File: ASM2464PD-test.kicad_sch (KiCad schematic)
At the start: 19 parts, among them J1 USB_C_Receptacle, J2 Bus_M.2_Socket_M

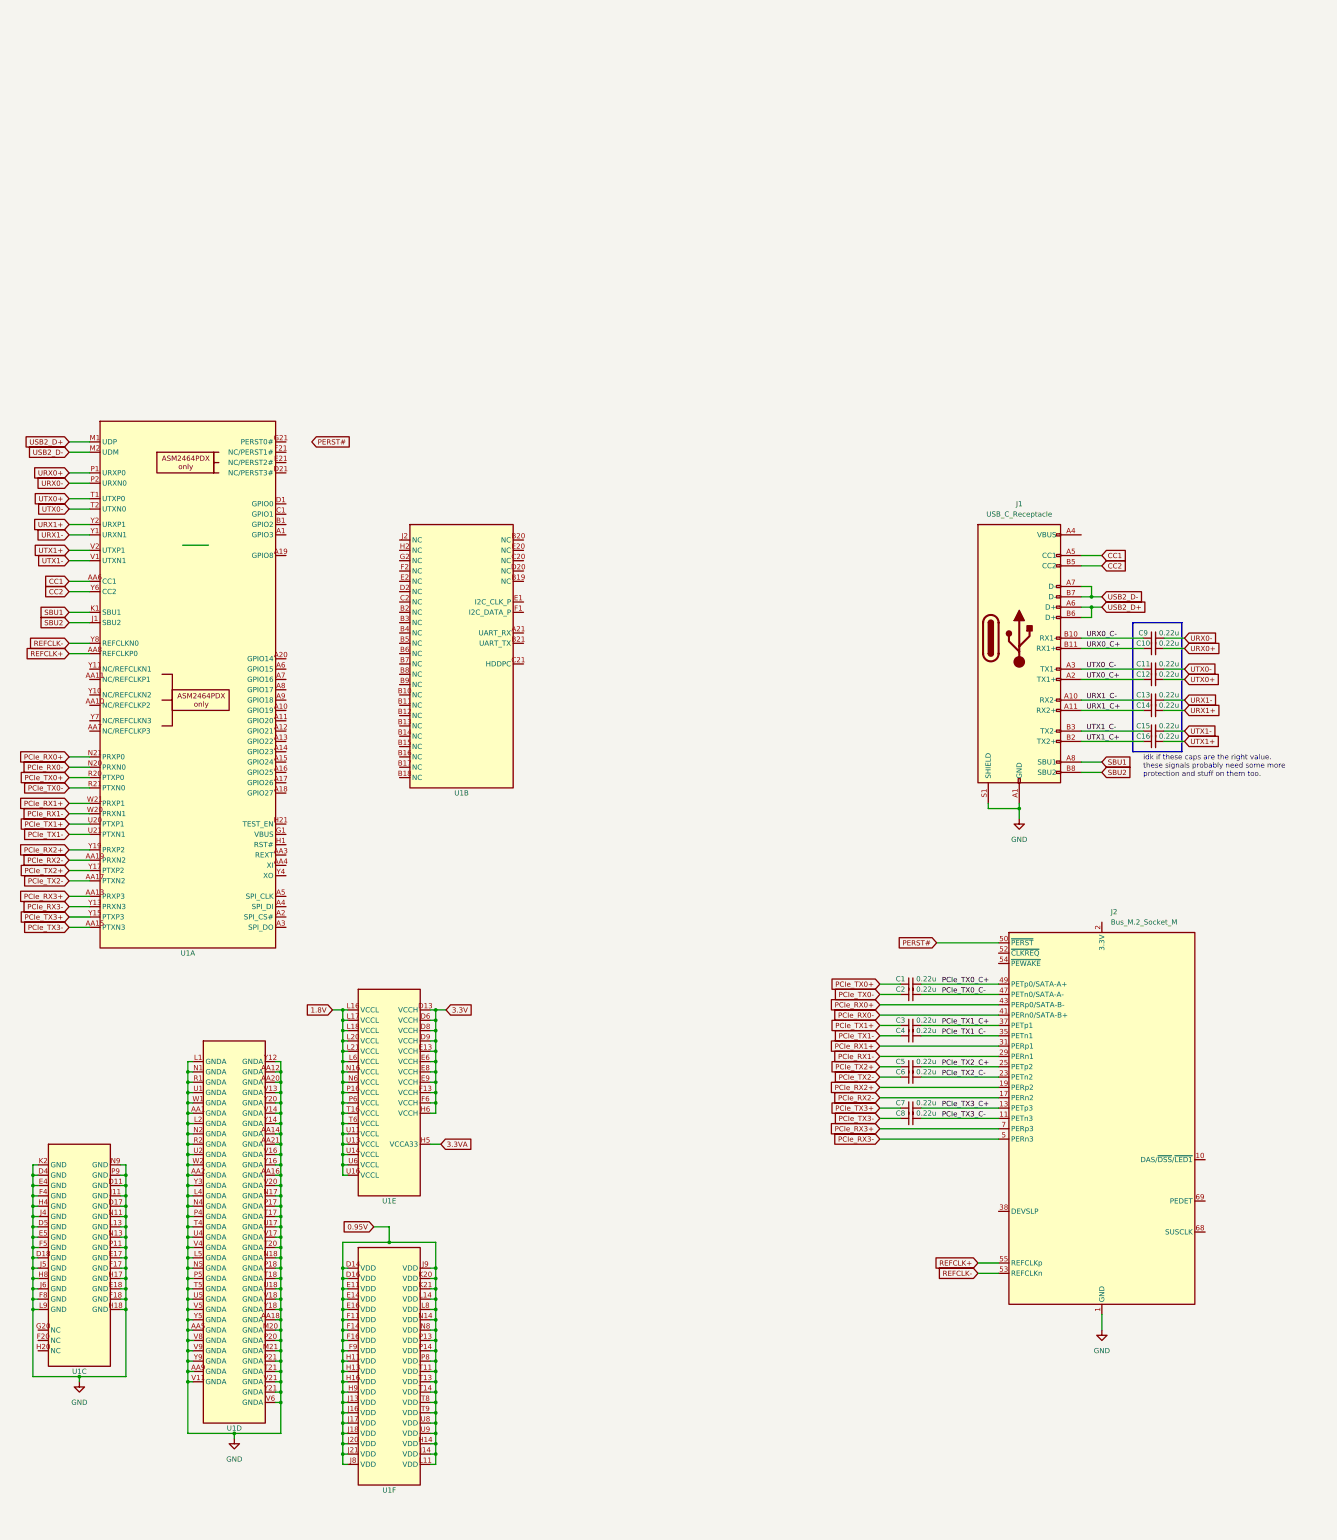
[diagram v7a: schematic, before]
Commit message: Updated schematic and rerouted some stuff
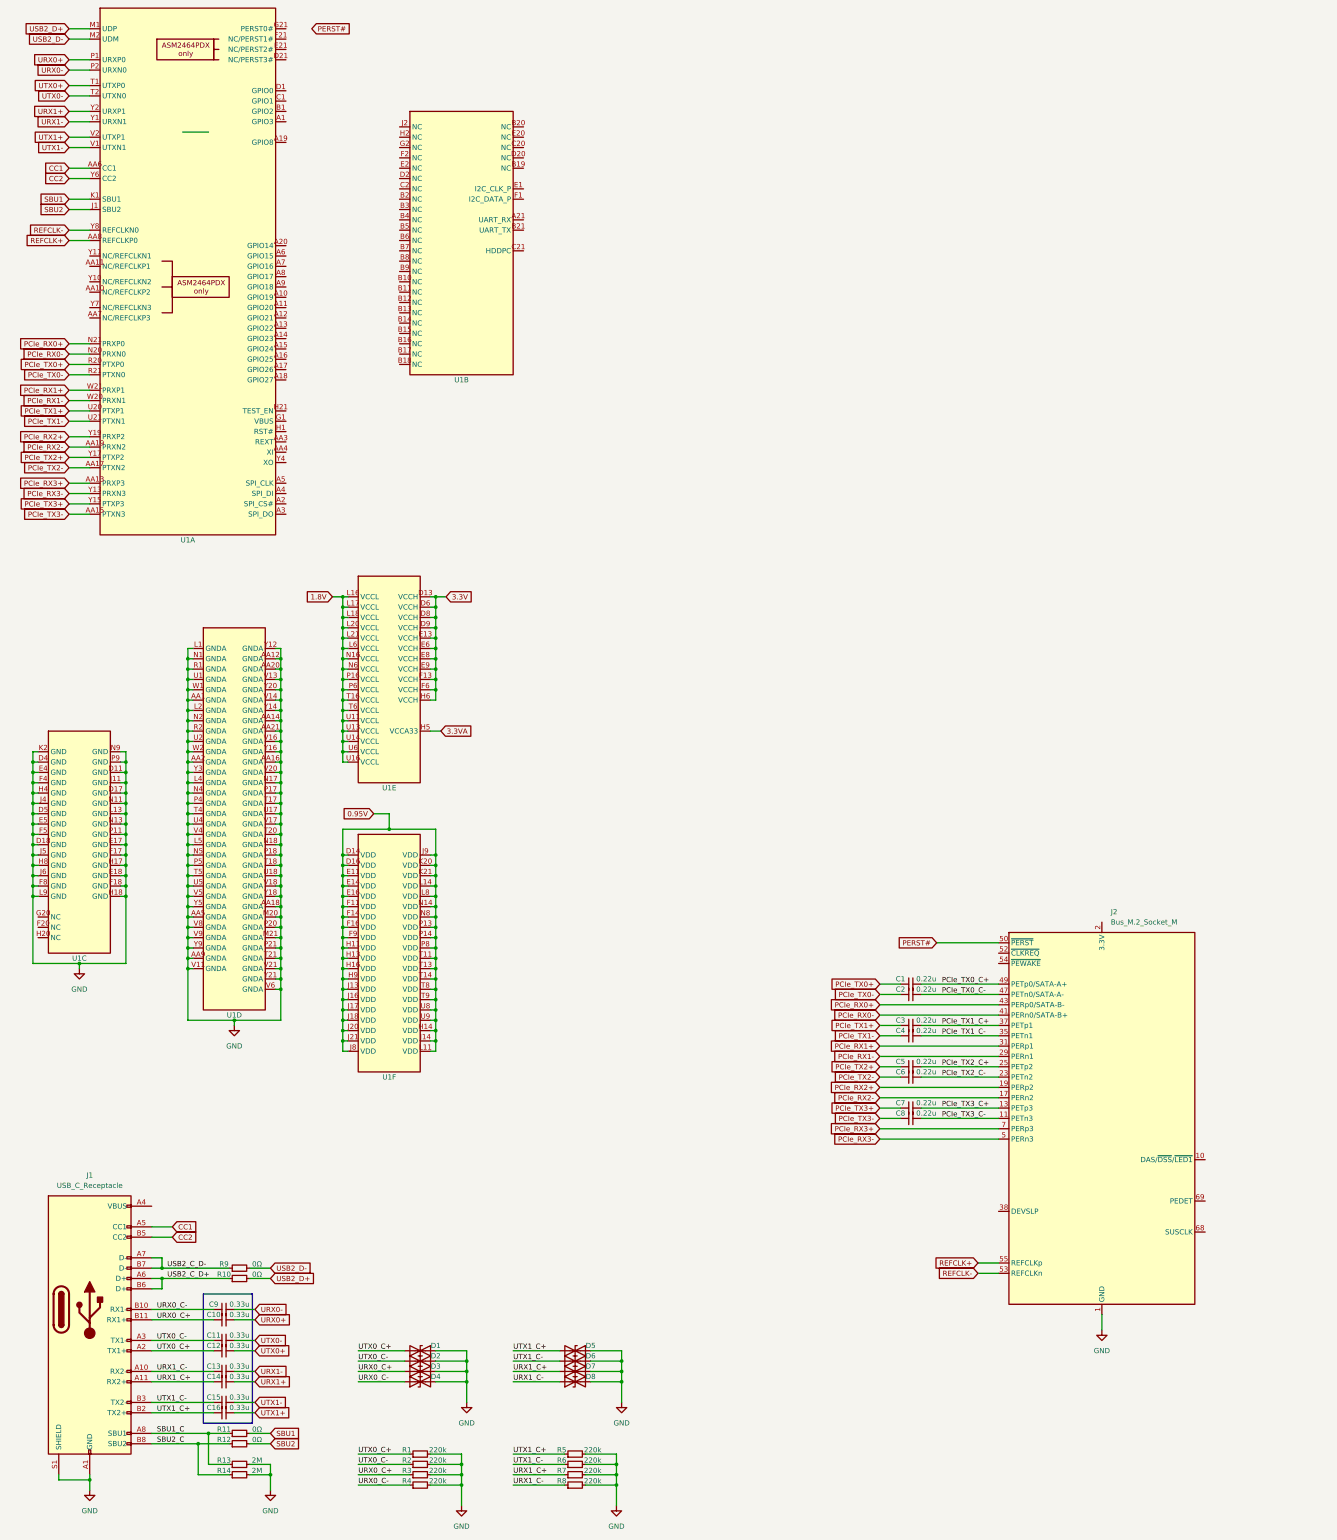
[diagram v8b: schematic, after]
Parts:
- added D1, D2, D3, D4, D5, D6, D7, D8: ~, Diode_SMD:D_0201_0603Metric, symbol Diode:ESD9B3.3ST5G
- added R1, R2, R3, R4, R5, R6, R7, R8: 220k, Resistor_SMD:R_0201_0603Metric, symbol Device:R_Small
- added R10, R11, R12, R9: 0Ω, Resistor_SMD:R_0201_0603Metric, symbol Device:R_Small
- added R13, R14: 2M, Resistor_SMD:R_0201_0603Metric, symbol Device:R_Small
- C10, C11, C12, C13, C14, C15, C16, C9: value 0.22u -> 0.33u; footprint Capacitor_SMD:C_0402_1005Metric -> Capacitor_SMD:C_0201_0603Metric
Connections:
- net GND: now also D1.2 (A2), D2.2 (A2), D3.2 (A2), D4.2 (A2), D5.2 (A2), D6.2 (A2), D7.2 (A2), D8.2 (A2), R1.2, R13.2, R14.2, R2.2, R3.2, R4.2, R5.2, R6.2, R7.2, R8.2
- net SBU1: now also R11.2; no longer J1.A8 (SBU1)
- net SBU2: now also R12.2; no longer J1.B8 (SBU2)
- net URX0_C+: now also D3.1 (A1), R3.1
- net URX0_C-: now also D4.1 (A1), R4.1
- net URX1_C+: now also D7.1 (A1), R7.1
- net URX1_C-: now also D8.1 (A1), R8.1
- net USB2_D+: now also R10.2; no longer J1.A6 (D+), J1.B6 (D+)
- net USB2_D-: now also R9.2; no longer J1.A7 (D-), J1.B7 (D-)
- net UTX0_C+: now also D1.1 (A1), R1.1
- net UTX0_C-: now also D2.1 (A1), R2.1
- net UTX1_C+: now also D5.1 (A1), R5.1
- net UTX1_C-: now also D6.1 (A1), R6.1
- new net SBU1_C: J1.A8 (SBU1), R11.1, R13.1
- new net SBU2_C: J1.B8 (SBU2), R12.1, R14.1
- new net USB2_C_D+: J1.A6 (D+), J1.B6 (D+), R10.1
- new net USB2_C_D-: J1.A7 (D-), J1.B7 (D-), R9.1
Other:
- note removed: "idk if these caps are the right value. these signals probably need some more protection and stuff on them too."
- moved on the sheet: C9, J1, U1A, U1B, U1C, U1D, U1E, U1F
